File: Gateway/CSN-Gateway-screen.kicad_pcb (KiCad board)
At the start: 2 copper layers, 32 x 58 mm, 27 parts, among them IC2 FT232RL, P1 USB_MINI, P2 CONN_01X12, P4 CONN_OLED_SCREEN, SW1 SW_PUSH, SW2 SW_PUSH

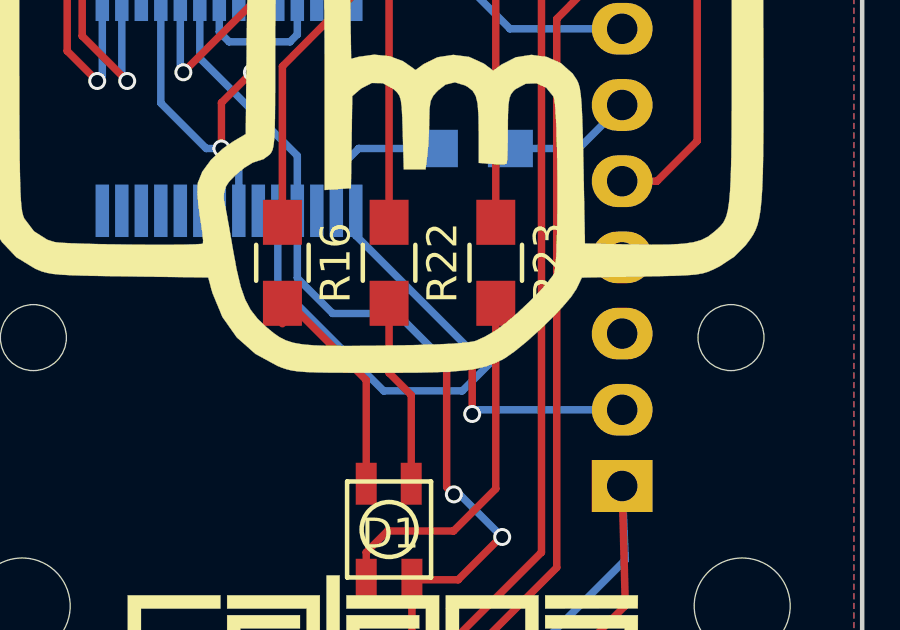
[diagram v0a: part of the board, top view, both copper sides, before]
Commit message: Fix footprints for power supply components
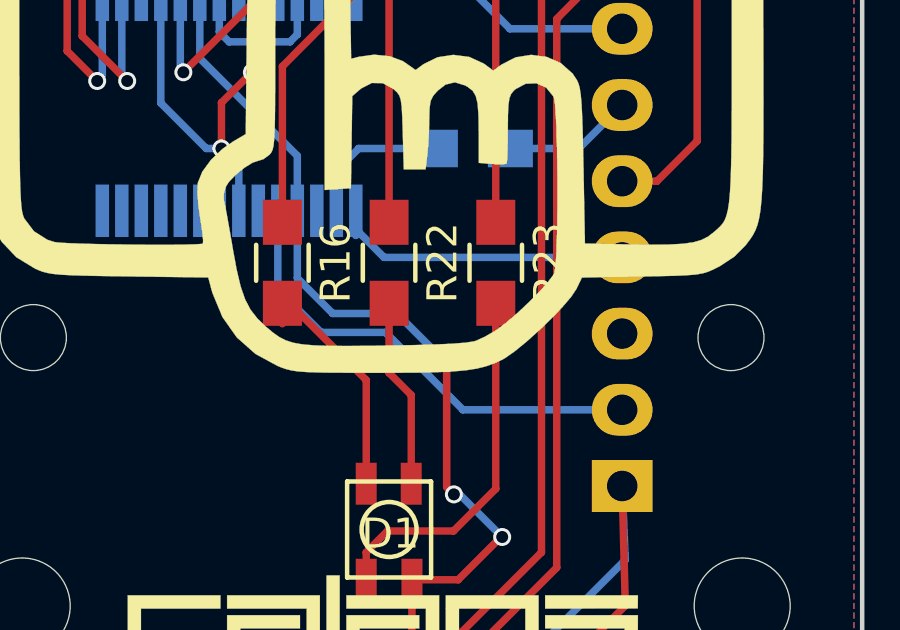
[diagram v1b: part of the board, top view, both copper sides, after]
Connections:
- P2 pad 2: RXI -> TXO
- P2 pad 4: TXO -> RXI
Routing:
- net RXI: track 13.5 -> 11.6 mm, vias 2 -> 0
- net TXO: track 17.3 -> 15.8 mm
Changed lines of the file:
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@@
     (area 109.424999 63.924999 141.575001 122.075001)
     (thickness 1.6)
-    (drawings 21)
-    (tracks 195)
+    (drawings 29)
+    (tracks 192)
     (zones 0)
     (modules 27)
@@
     (32 B.Adhes user)
     (33 F.Adhes user)
-    (34 B.Paste user)
+    (34 B.Paste user hide)
     (35 F.Paste user)
     (36 B.SilkS user)
-    (37 F.SilkS user)
+    (37 F.SilkS user hide)
     (38 B.Mask user)
     (39 F.Mask user)
@@
       (net 2 VCC))
     (pad 2 thru_hole oval (at 0 -2.54) (size 2.032 1.7272) (drill 1.016) (layers *.Cu *.Mask)
+      (net 12 TXO))
+    (pad 3 thru_hole oval (at 0 -5.08) (size 2.032 1.7272) (drill 1.016) (layers *.Cu *.Mask)
+      (net 3 GND))
+    (pad 4 thru_hole oval (at 0 -7.62) (size 2.032 1.7272) (drill 1.016) (layers *.Cu *.Mask)
       (net 11 RXI))
-    (pad 3 thru_hole oval (at 0 -5.08) (size 2.032 1.7272) (drill 1.016) (layers *.Cu *.Mask)
-      (net 3 GND))
-    (pad 4 thru_hole oval (at 0 -7.62) (size 2.032 1.7272) (drill 1.016) (layers *.Cu *.Mask)
-      (net 12 TXO))
     (pad 5 thru_hole oval (at 0 -10.16) (size 2.032 1.7272) (drill 1.016) (layers *.Cu *.Mask)
       (net 13 SCL))
@@
   (segment (start 123.971 95.993) (end 123.971 97.326) (width 0.25) (layer B.Cu) (net 1))
   (segment (start 124.714 95.25) (end 123.971 95.993) (width 0.25) (layer B.Cu) (net 1))
-  (segment (start 126.492 109.626) (end 126.492 111.76) (width 0.25) (layer F.Cu) (net 2))
-  (segment (start 126.492 111.76) (end 124.968 113.284) (width 0.25) (layer F.Cu) (net 2))
-  (segment (start 126.492 109.626) (end 128.034 109.626) (width 0.25) (layer F.Cu) (net 2))
   (segment (start 122.671 99.571) (end 122.671 97.326) (width 0.25) (layer B.Cu) (net 2))
   (segment (start 123.85 100.75) (end 122.671 99.571) (width 0.25) (layer B.Cu) (net 2))
@@
   (via (at 129.5 108.2) (size 0.6) (drill 0.4) (layers F.Cu B.Cu) (net 2))
   (segment (start 129.46 108.2) (end 129.5 108.2) (width 0.25) (layer F.Cu) (net 2))
-  (segment (start 128.034 109.626) (end 129.46 108.2) (width 0.25) (layer F.Cu) (net 2))
   (segment (start 119.614 85.344) (end 119.614 84.886) (width 0.25) (layer B.Cu) (net 2))
   (segment (start 119.614 84.886) (end 124.206 80.294) (width 0.25) (layer B.Cu) (net 2))
@@
   (segment (start 112.522 115.824) (end 119.022 115.824) (width 0.25) (layer F.Cu) (net 2))
   (segment (start 119.022 115.824) (end 121.562 113.284) (width 0.25) (layer F.Cu) (net 2))
-  (segment (start 121.562 113.284) (end 124.968 113.284) (width 0.25) (layer F.Cu) (net 2))
-  (via (at 124.968 113.284) (size 0.6) (drill 0.4) (layers F.Cu B.Cu) (net 2))
   (segment (start 133.604 108.966) (end 133.5 106.5) (width 0.25) (layer B.Cu) (net 2) (status 20))
   (segment (start 129.286 113.284) (end 133.604 108.966) (width 0.25) (layer B.Cu) (net 2))
-  (segment (start 124.968 113.284) (end 129.286 113.284) (width 0.25) (layer B.Cu) (net 2))
   (segment (start 131.572 115.824) (end 138.072 115.824) (width 0.25) (layer F.Cu) (net 2))
   (segment (start 131.572 115.824) (end 131.572 112.522) (width 0.25) (layer F.Cu) (net 2))
   (segment (start 133.604 110.49) (end 133.5 106.5) (width 0.25) (layer F.Cu) (net 2) (status 20))
   (segment (start 131.572 112.522) (end 133.604 110.49) (width 0.25) (layer F.Cu) (net 2))
+  (segment (start 128.034 109.626) (end 129.46 108.2) (width 0.25) (layer F.Cu) (net 2))
+  (segment (start 121.562 113.284) (end 124.968 113.284) (width 0.25) (layer F.Cu) (net 2))
+  (segment (start 124.968 113.284) (end 129.286 113.284) (width 0.25) (layer B.Cu) (net 2))
+  (segment (start 126.492 109.626) (end 126.492 111.76) (width 0.25) (layer F.Cu) (net 2))
+  (segment (start 126.492 111.76) (end 124.968 113.284) (width 0.25) (layer F.Cu) (net 2))
+  (segment (start 126.492 109.626) (end 128.034 109.626) (width 0.25) (layer F.Cu) (net 2))
+  (via (at 124.968 113.284) (size 0.6) (drill 0.4) (layers F.Cu B.Cu) (net 2))
   (segment (start 120.5 72.5) (end 120.5 75.953) (width 0.25) (layer B.Cu) (net 3))
   (segment (start 120.5 75.953) (end 121.666 77.119) (width 0.25) (layer B.Cu) (net 3))
@@
   (segment (start 124.968 102.968) (end 124.968 106.426) (width 0.25) (layer F.Cu) (net 10))
   (segment (start 122.174 100.41) (end 122.174 101.092) (width 0.25) (layer F.Cu) (net 10))
+  (segment (start 124.621 97.326) (end 124.621 97.941) (width 0.25) (layer B.Cu) (net 11))
+  (segment (start 124.621 97.941) (end 125.56 98.88) (width 0.25) (layer B.Cu) (net 11))
+  (segment (start 125.56 98.88) (end 133.5 98.88) (width 0.25) (layer B.Cu) (net 11))
   (segment (start 124.621 97.326) (end 124.621 98.151) (width 0.25) (layer B.Cu) (net 11))
-  (segment (start 124.621 98.151) (end 128.52 102.05) (width 0.25) (layer B.Cu) (net 11))
-  (via (at 128.52 102.05) (size 0.6) (drill 0.4) (layers F.Cu B.Cu) (net 11))
-  (segment (start 128.52 102.05) (end 128.5 102.07) (width 0.25) (layer F.Cu) (net 11))
-  (segment (start 128.5 102.07) (end 128.5 104.1) (width 0.25) (layer F.Cu) (net 11))
-  (via (at 128.5 104.1) (size 0.6) (drill 0.4) (layers F.Cu B.Cu) (net 11))
-  (segment (start 128.5 104.1) (end 128.64 103.96) (width 0.25) (layer B.Cu) (net 11))
-  (segment (start 128.64 103.96) (end 133.5 103.96) (width 0.25) (layer B.Cu) (net 11))
-  (segment (start 122.021 97.326) (end 122.021 99.801) (width 0.25) (layer B.Cu) (net 12))
-  (segment (start 128.17 103.33) (end 132.62 98.88) (width 0.25) (layer B.Cu) (net 12))
-  (segment (start 125.55 103.33) (end 128.17 103.33) (width 0.25) (layer B.Cu) (net 12))
-  (segment (start 122.021 99.801) (end 125.55 103.33) (width 0.25) (layer B.Cu) (net 12))
-  (segment (start 132.62 98.88) (end 133.5 98.88) (width 0.25) (layer B.Cu) (net 12))
+  (segment (start 132.62 98.88) (end 133.5 98.88) (width 0.25) (layer B.Cu) (net 11))
+  (segment (start 122.021 97.326) (end 122.021 99.941) (width 0.25) (layer B.Cu) (net 12))
+  (segment (start 128.19 103.96) (end 133.5 103.96) (width 0.25) (layer B.Cu) (net 12))
+  (segment (start 125.61 101.38) (end 128.19 103.96) (width 0.25) (layer B.Cu) (net 12))
+  (segment (start 123.46 101.38) (end 125.61 101.38) (width 0.25) (layer B.Cu) (net 12))
+  (segment (start 122.021 99.941) (end 123.46 101.38) (width 0.25) (layer B.Cu) (net 12))
   (segment (start 133.5 96.34) (end 134.66 96.34) (width 0.25) (layer F.Cu) (net 13))
   (segment (start 128.365 75.5) (end 126.746 77.119) (width 0.25) (layer F.Cu) (net 13))
@@
   (segment (start 131.572 83.058) (end 131.572 81.026) (width 0.25) (layer F.Cu) (net 19))
   (segment (start 122.174 92.513998) (end 131.572 83.058) (width 0.25) (layer F.Cu) (net 19))
-  (segment (start 129.286 100.41) (end 129.286 106.594) (width 0.25) (layer F.Cu) (net 34))
   (segment (start 124.968 108.712) (end 124.968 109.626) (width 0.25) (layer F.Cu) (net 34))
   (segment (start 125.68 108) (end 124.968 108.712) (width 0.25) (layer F.Cu) (net 34))
   (segment (start 127.88 108) (end 125.68 108) (width 0.25) (layer F.Cu) (net 34))
+  (segment (start 124.968 109.626) (end 124.968 109.878) (width 0.25) (layer F.Cu) (net 34))
   (segment (start 129.286 106.594) (end 127.88 108) (width 0.25) (layer F.Cu) (net 34))
-  (segment (start 124.968 109.626) (end 124.968 109.878) (width 0.25) (layer F.Cu) (net 34))
+  (segment (start 129.286 100.41) (end 129.286 106.594) (width 0.25) (layer F.Cu) (net 34))
   (zone (net 3) (net_name GND) (layer F.Cu) (hatch edge 0.508)
     (connect_pads (clearance 0.508))

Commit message: new pcb for v1.1 prototype
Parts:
- removed C2: 0.1uF, Capacitors_SMD:C_0805_HandSoldering
- removed the G*** at (125.2, 92.0)
- removed R20: 4k7, Resistors_SMD:R_0805_HandSoldering
- removed R21: 10k, Resistors_SMD:R_0805_HandSoldering
- added C1: 100nF, Capacitors_SMD:C_0805_HandSoldering, F.Cu at (115.6, 87.2)
- C19: value 100nF -> 10uF; footprint Capacitors_SMD:C_0805_HandSoldering -> Capacitors_Tantalum_SMD:CP_Tantalum_Case-R_EIA-2012-12_Hand
- P2: footprint Pin_Headers:Pin_Header_Straight_1x12 -> Connectors:IDC_Header_Straight_12pins
- R16, R22, R23: value 100 -> 1K
- moved P2 21.9 mm to (130.6, 84.8), turned to 270 degrees
- moved IC2 8.55 mm to (117.2, 85.8)
- moved C19 8.26 mm to (116.9, 95.5)
- moved C15 7.51 mm to (116.9, 92.7)
- moved R16 5.68 mm to (119.8, 104.2), turned to 0 degrees
- moved R23 5.68 mm to (131.7, 104.2), turned to 0 degrees
- moved R22 5.14 mm to (125.7, 104.2), turned to 0 degrees
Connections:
- C15 pad 1: VCC -> Net-(C15-Pad1)
- C19 pad 1: VCC -> Net-(C15-Pad1)
- IC2 pad 10: Net-(IC2-Pad10) -> (no net)
- IC2 pad 11: Net-(IC2-Pad11) -> (no net)
- IC2 pad 12: Net-(IC2-Pad12) -> (no net)
- IC2 pad 13: Net-(IC2-Pad13) -> (no net)
- IC2 pad 14: Net-(IC2-Pad14) -> (no net)
- IC2 pad 19: Net-(IC2-Pad19) -> (no net)
- IC2 pad 2: Net-(C2-Pad2) -> RST
- IC2 pad 20: VCC -> Net-(C15-Pad1)
- IC2 pad 22: Net-(IC2-Pad22) -> (no net)
- IC2 pad 23: Net-(IC2-Pad23) -> (no net)
- IC2 pad 27: Net-(IC2-Pad27) -> (no net)
- IC2 pad 28: Net-(IC2-Pad28) -> (no net)
- IC2 pad 3: Net-(IC2-Pad3) -> (no net)
- IC2 pad 4: VCC -> Net-(C15-Pad1)
- IC2 pad 6: Net-(IC2-Pad6) -> (no net)
- IC2 pad 9: Net-(IC2-Pad9) -> (no net)
- P1 pad 1: Net-(P1-Pad1) -> Net-(C15-Pad1)
- P1 pad 4: Net-(P1-Pad4) -> (no net)
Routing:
- net GND: track 55.3 -> 163.4 mm, vias 2 -> 6
- net Net-(C15-Pad1): track 0.00 -> 36.3 mm, vias 0 -> 2
- net SCL: track 38.9 -> 18.3 mm
- net Net-(P1-Pad1): track 20.3 -> 0.00 mm, vias 1 -> 0
- net Net-(IC2-Pad19): track 12.2 -> 0.00 mm, vias 2 -> 0
- net RGB1: track 23.7 -> 13.6 mm
- net RGB2: track 20.2 -> 10.1 mm
- net VCC: track 89.5 -> 79.8 mm, vias 4 -> 3
- net Net-(IC2-Pad15): track 31.4 -> 22.3 mm
- net Net-(IC2-Pad16): track 31.7 -> 23.3 mm
- net BTN2: track 51.4 -> 44.9 mm, vias 0 -> 2
- net Net-(C1-Pad2): track 0.00 -> 5.03 mm, vias 0 -> 1
- net Net-(C2-Pad2): track 4.94 -> 0.00 mm
- net RST: track 4.81 -> 9.62 mm, vias 0 -> 1
- net Net-(D1-Pad4): track 6.32 -> 2.48 mm
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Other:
- board text added: "Gateway v1.1"
- board text removed: "BTN1"
- board text removed: "BTN2"
- board text removed: "Gateway v1.0"
- board text removed: "RGB1"
- board text removed: "RGB2"
- board text removed: "RGB3"
- board text removed: "RST"
- board text removed: "RXI"
- board text removed: "TXO"

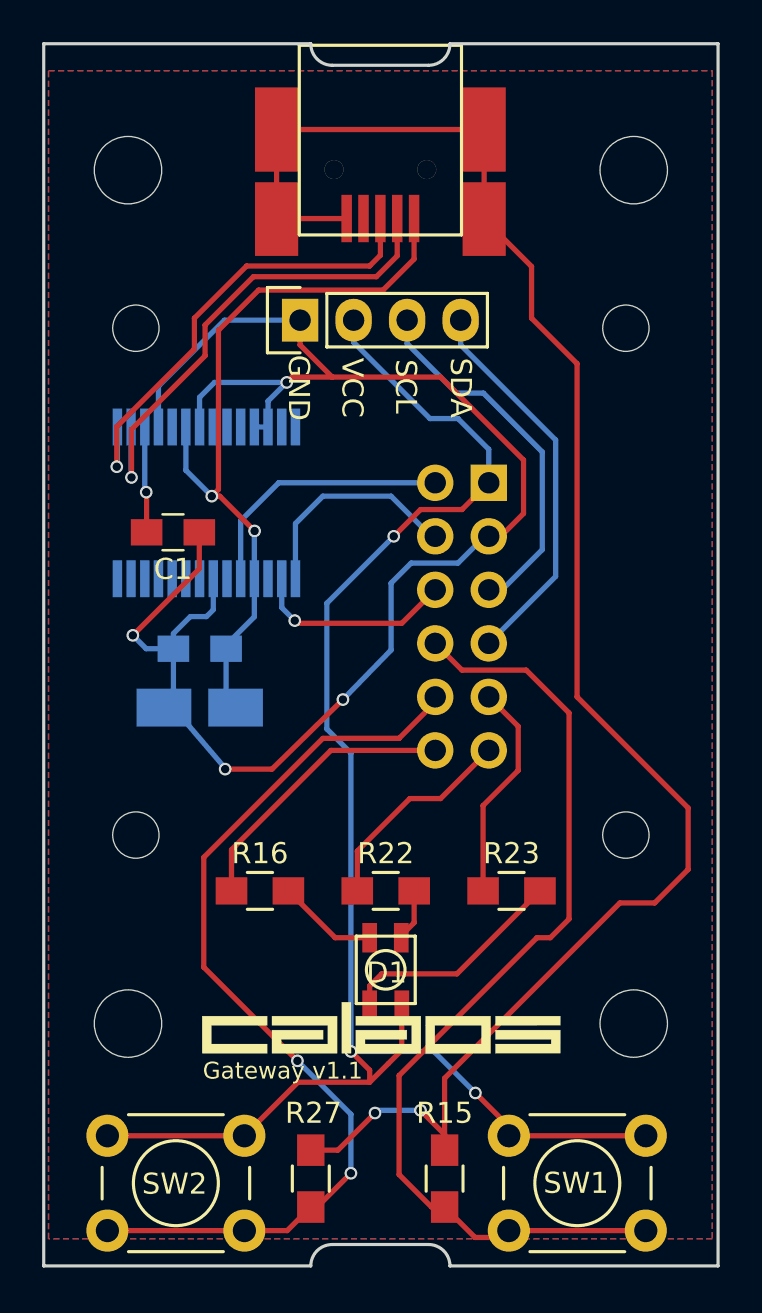
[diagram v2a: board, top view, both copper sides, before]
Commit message: add missing logo to screen pcb
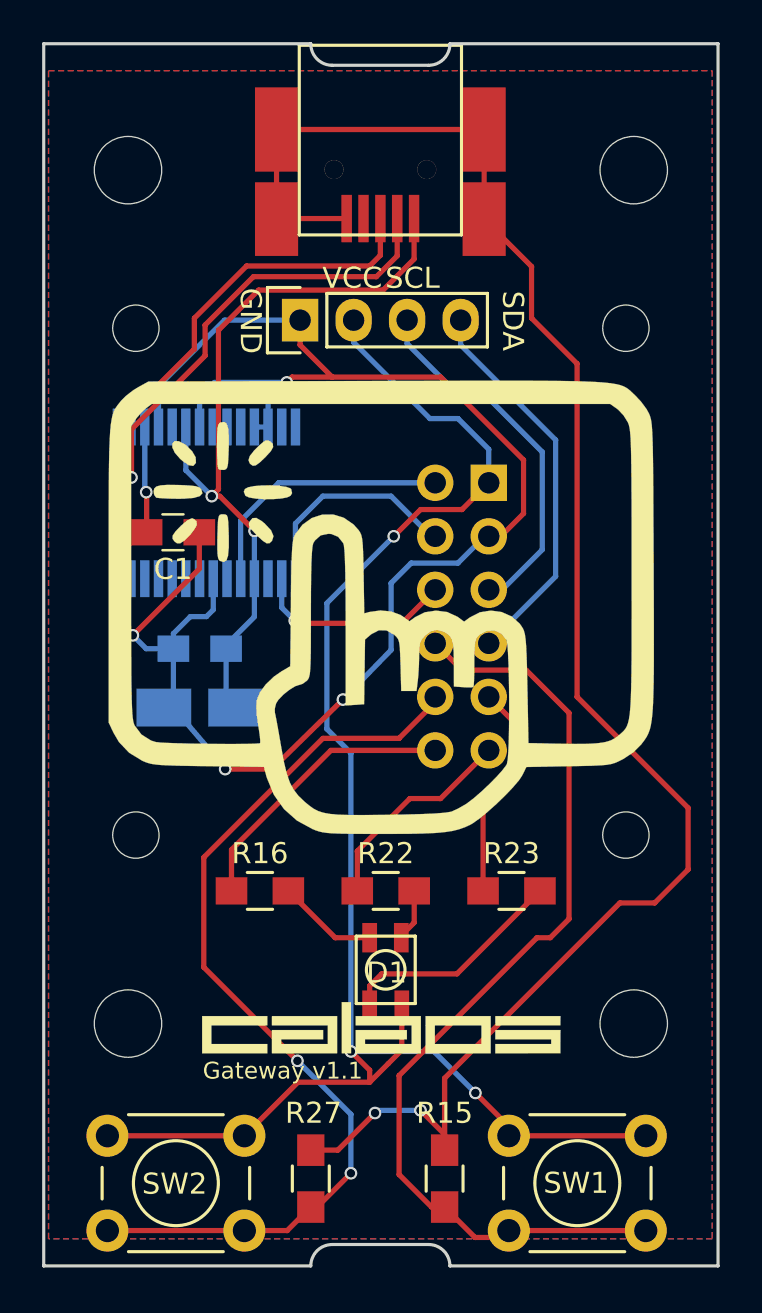
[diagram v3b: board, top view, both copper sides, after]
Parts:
- added G***: LOGO, libs:calaos_logo_small, F.Cu at (125.5, 90.7)

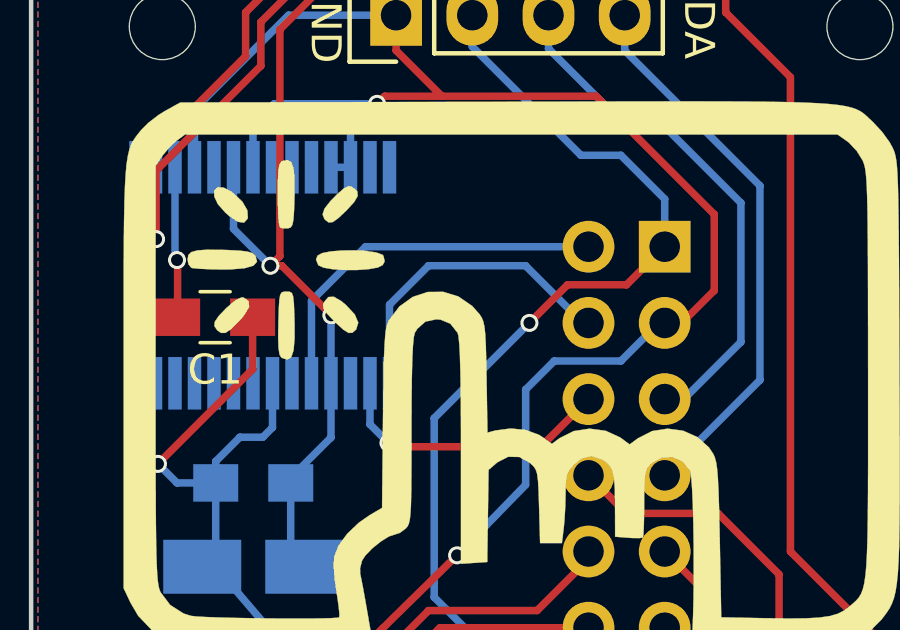
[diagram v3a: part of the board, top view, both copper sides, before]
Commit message: Fix wrong reset pin for ICSP, fix exchange of rx/tx in ftdi
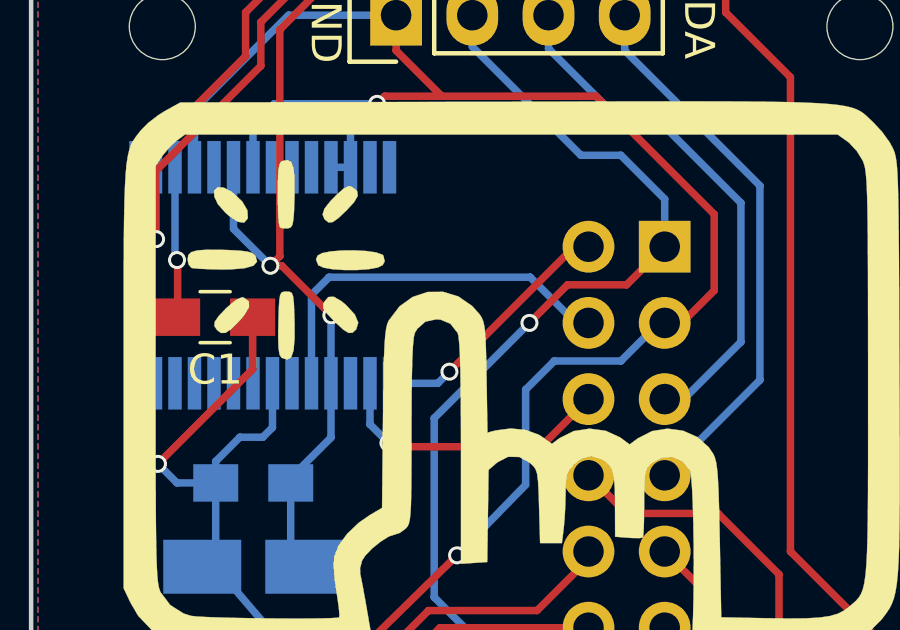
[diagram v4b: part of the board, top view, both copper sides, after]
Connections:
- IC2 pad 1: RXI -> TXO
- IC2 pad 5: TXO -> RXI
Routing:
- net TXO: track 12.7 -> 8.52 mm, vias 0 -> 1
- net RXI: track 10.6 -> 13.2 mm
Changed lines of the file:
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@@
 (kicad_pcb (version 4) (host pcbnew 4.0.4-stable)
   (general
-    (links 0)
+    (links 46)
     (no_connects 0)
     (area 109.424999 63.924999 141.575001 122.075001)
     (thickness 1.6)
     (drawings 17)
-    (tracks 218)
+    (tracks 221)
     (zones 0)
     (modules 25)
@@
     (34 B.Paste user)
     (35 F.Paste user)
-    (36 B.SilkS user)
-    (37 F.SilkS user)
+    (36 B.SilkS user hide)
+    (37 F.SilkS user hide)
     (38 B.Mask user)
     (39 F.Mask user)
@@
     (fp_line (start -2.875 4.75) (end -4.475 4.75) (layer B.SilkS) (width 0.15))
     (pad 1 smd rect (at -3.6 4.225 90) (size 1.75 0.45) (layers B.Cu B.Paste B.Mask)
-      (net 8 RXI))
+      (net 9 TXO))
     (pad 2 smd rect (at -3.6 3.575 90) (size 1.75 0.45) (layers B.Cu B.Paste B.Mask)
       (net 5 RST))
@@
       (net 19 "Net-(C15-Pad1)"))
     (pad 5 smd rect (at -3.6 1.625 90) (size 1.75 0.45) (layers B.Cu B.Paste B.Mask)
-      (net 9 TXO))
+      (net 8 RXI))
     (pad 6 smd rect (at -3.6 0.975 90) (size 1.75 0.45) (layers B.Cu B.Paste B.Mask))
     (pad 7 smd rect (at -3.6 0.325 90) (size 1.75 0.45) (layers B.Cu B.Paste B.Mask)
@@
   (segment (start 124.968 106.426) (end 123.3335 106.426) (width 0.25) (layer F.Cu) (net 7))
   (segment (start 123.3335 106.426) (end 121.111 104.2035) (width 0.25) (layer F.Cu) (net 7))
+  (segment (start 128.0795 87.376) (end 127.6604 87.376) (width 0.25) (layer B.Cu) (net 8))
+  (segment (start 127.6604 87.376) (end 126.1364 85.852) (width 0.25) (layer B.Cu) (net 8))
+  (segment (start 118.846 86.4368) (end 118.846 89.3885) (width 0.25) (layer B.Cu) (net 8))
+  (segment (start 119.4308 85.852) (end 118.846 86.4368) (width 0.25) (layer B.Cu) (net 8))
+  (segment (start 126.1364 85.852) (end 119.4308 85.852) (width 0.25) (layer B.Cu) (net 8))
   (segment (start 128.0795 87.376) (end 127.889 87.376) (width 0.25) (layer B.Cu) (net 8))
-  (segment (start 127.889 87.376) (end 125.984 85.471) (width 0.25) (layer B.Cu) (net 8))
-  (segment (start 125.984 85.471) (end 122.7455 85.471) (width 0.25) (layer B.Cu) (net 8))
-  (segment (start 122.7455 85.471) (end 121.446 86.7705) (width 0.25) (layer B.Cu) (net 8))
-  (segment (start 121.446 86.7705) (end 121.446 89.3885) (width 0.25) (layer B.Cu) (net 8))
-  (segment (start 128.0795 84.836) (end 120.65 84.836) (width 0.25) (layer B.Cu) (net 9))
-  (segment (start 118.846 86.64) (end 118.846 89.3885) (width 0.25) (layer B.Cu) (net 9))
-  (segment (start 120.65 84.836) (end 118.846 86.64) (width 0.25) (layer B.Cu) (net 9))
+  (segment (start 121.446 89.3885) (end 123.0571 89.3885) (width 0.25) (layer B.Cu) (net 9))
+  (segment (start 123.444 89.0016) (end 127.6096 84.836) (width 0.25) (layer F.Cu) (net 9))
+  (via (at 123.444 89.0016) (size 0.6) (drill 0.4) (layers F.Cu B.Cu) (net 9))
+  (segment (start 123.0571 89.3885) (end 123.444 89.0016) (width 0.25) (layer B.Cu) (net 9))
+  (segment (start 127.6096 84.836) (end 128.0795 84.836) (width 0.25) (layer F.Cu) (net 9))
   (segment (start 126.746 77.119) (end 126.746 78.232) (width 0.25) (layer B.Cu) (net 10))
   (segment (start 133.1595 88.011) (end 131.2545 89.916) (width 0.25) (layer B.Cu) (net 10))
